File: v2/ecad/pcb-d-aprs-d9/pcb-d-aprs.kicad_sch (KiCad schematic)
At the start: 207 parts, among them K1 Omron G6K-2F-Y 5 VDC DPDT sig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, Q1 2N7002 PA_EN -> H/L low (neve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, Q2 2N7002 relay coil, Q3 2N7002, Q4 2N7002, Q5 2N7002, Q6 2N7002, Q7 2N7002, Q8 2N7002, Q9 2N7002, U1 TLV75533PDBV 3.3 V 500 mA LDO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, U10 74LVC1G08 AND: headsets AND s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, U11 74LVC1G04 inverter (2 A 4 Y):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, U12 74LVC1G08 AND: KEY = PTT_ANY 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, U13 74LVC1G04 inverter: KEY -> SA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, U14 74LVC1G08 AND: PA_KEY = KEY A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, U15 TPS22810DRV, U16 PCA9555PW 0x26: COS, PTT stat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, U2 NiceRF SA868 VHF 2 W exciter,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, U3 CP2102N-A02-GQFN28 USB-UART b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, U4 TUSB2046BI four-port USB 2.0 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, U5 USBLC6-2SC6, U6 TI PCM2912A USB audio codec (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, U7 TI TPA6132A2 headphone amplif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, U8 TLV9062IDGK dual op amp (1 OU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, U9 74LVC1G08 AND (1 A 2 B 3 GND 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, Y1 6 MHz 3225 (CL 20 pF; C1 = C2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, Y2 6 MHz 3225 (codec clock; 18 p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

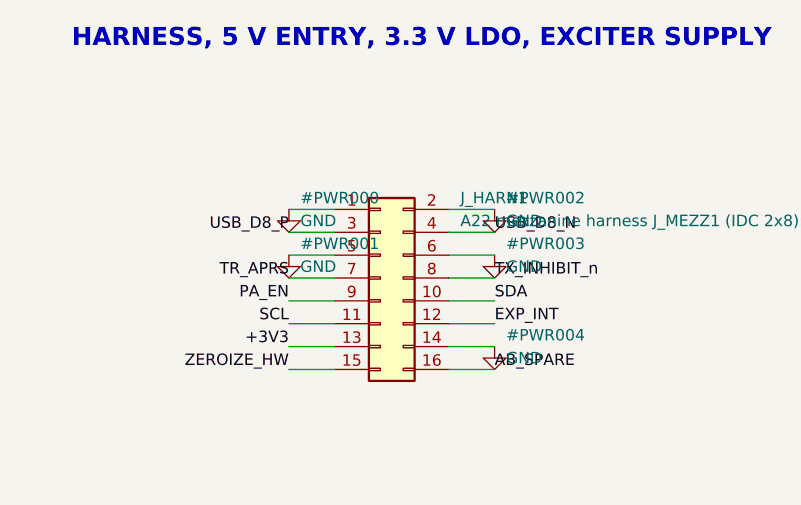
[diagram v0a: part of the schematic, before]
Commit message: feat(d): D's routed board and its regenerated schematic, tracked [MESHSAT-862]
The board is the best of the D run: 0 hard of the fifteen types, 3 unrouted
before the finish (the finish closes two of them), 5 of 5 pairs laid and
every one within 1 mm, and the schematic carries the harness pin map that
moved USB_D8 to the header's end row.

It is committed as an artefact, not as a deliverable: a routed board that
exists only in a rented box's copy directory exists nowhere, which is how
four of them were lost on 10 September. The one open and what it is are in
appendix 32.128.
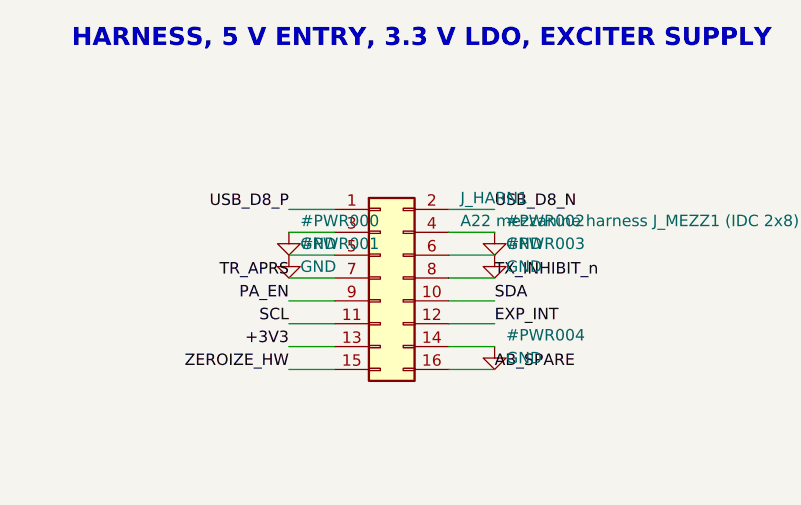
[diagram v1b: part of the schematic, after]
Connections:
- net GND: now also J_HARN1.3 (Pin_3), J_HARN1.4 (Pin_4); no longer J_HARN1.1 (Pin_1), J_HARN1.2 (Pin_2)
- net USB_D8_N: now also J_HARN1.2 (Pin_2); no longer J_HARN1.4 (Pin_4)
- net USB_D8_P: now also J_HARN1.1 (Pin_1); no longer J_HARN1.3 (Pin_3)
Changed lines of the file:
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@@
 	)
 	(wire (pts (xy 34.29 43.18) (xy 29.21 43.18)) (stroke (width 0) (type default)))
-	(symbol (lib_id "power:GND") (at 29.21 43.18 0) (unit 1) (exclude_from_sim no) (in_bom no) (on_board no) (dnp no) (fields_autoplaced yes)
-		(property "Reference" "#PWR000" (at 30.48 41.91 0) (effects (font (size 1.27 1.27)) (justify left)))
-		(property "Value" "GND" (at 30.48 44.45 0) (effects (font (size 1.27 1.27)) (justify left)))
-		(property "Footprint" "" (at 29.21 43.18 0) (effects (font (size 1.27 1.27)) (justify left) (hide yes)))
-		(property "Datasheet" "" (at 29.21 43.18 0) (effects (font (size 1.27 1.27)) (justify left) (hide yes)))
-		(property "Description" "" (at 29.21 43.18 0) (effects (font (size 1.27 1.27)) (justify left) (hide yes)))
+	(label "USB_D8_P" (at 29.21 43.18 180) (fields_autoplaced yes) (effects (font (size 1.27 1.27)) (justify right bottom)))
+	(wire (pts (xy 34.29 45.72) (xy 29.21 45.72)) (stroke (width 0) (type default)))
+	(symbol (lib_id "power:GND") (at 29.21 45.72 0) (unit 1) (exclude_from_sim no) (in_bom no) (on_board no) (dnp no) (fields_autoplaced yes)
+		(property "Reference" "#PWR000" (at 30.48 44.45 0) (effects (font (size 1.27 1.27)) (justify left)))
+		(property "Value" "GND" (at 30.48 46.99 0) (effects (font (size 1.27 1.27)) (justify left)))
+		(property "Footprint" "" (at 29.21 45.72 0) (effects (font (size 1.27 1.27)) (justify left) (hide yes)))
+		(property "Datasheet" "" (at 29.21 45.72 0) (effects (font (size 1.27 1.27)) (justify left) (hide yes)))
+		(property "Description" "" (at 29.21 45.72 0) (effects (font (size 1.27 1.27)) (justify left) (hide yes)))
 		(pin "1")
 		(instances (project "pcb-d-aprs" (path "/ba66a0ce-d686-5e81-bc86-e09a2b8c9d8d" (reference "#PWR000") (unit 1))))
 	)
-	(wire (pts (xy 34.29 45.72) (xy 29.21 45.72)) (stroke (width 0) (type default)))
-	(label "USB_D8_P" (at 29.21 45.72 180) (fields_autoplaced yes) (effects (font (size 1.27 1.27)) (justify right bottom)))
 	(wire (pts (xy 34.29 48.26) (xy 29.21 48.26)) (stroke (width 0) (type default)))
 	(symbol (lib_id "power:GND") (at 29.21 48.26 0) (unit 1) (exclude_from_sim no) (in_bom no) (on_board no) (dnp no) (fields_autoplaced yes)
@@
 	(label "ZEROIZE_HW" (at 29.21 60.96 180) (fields_autoplaced yes) (effects (font (size 1.27 1.27)) (justify right bottom)))
 	(wire (pts (xy 46.99 43.18) (xy 52.07 43.18)) (stroke (width 0) (type default)))
-	(symbol (lib_id "power:GND") (at 52.07 43.18 0) (unit 1) (exclude_from_sim no) (in_bom no) (on_board no) (dnp no) (fields_autoplaced yes)
-		(property "Reference" "#PWR002" (at 53.34 41.91 0) (effects (font (size 1.27 1.27)) (justify left)))
-		(property "Value" "GND" (at 53.34 44.45 0) (effects (font (size 1.27 1.27)) (justify left)))
-		(property "Footprint" "" (at 52.07 43.18 0) (effects (font (size 1.27 1.27)) (justify left) (hide yes)))
-		(property "Datasheet" "" (at 52.07 43.18 0) (effects (font (size 1.27 1.27)) (justify left) (hide yes)))
-		(property "Description" "" (at 52.07 43.18 0) (effects (font (size 1.27 1.27)) (justify left) (hide yes)))
+	(label "USB_D8_N" (at 52.07 43.18 0) (fields_autoplaced yes) (effects (font (size 1.27 1.27)) (justify left bottom)))
+	(wire (pts (xy 46.99 45.72) (xy 52.07 45.72)) (stroke (width 0) (type default)))
+	(symbol (lib_id "power:GND") (at 52.07 45.72 0) (unit 1) (exclude_from_sim no) (in_bom no) (on_board no) (dnp no) (fields_autoplaced yes)
+		(property "Reference" "#PWR002" (at 53.34 44.45 0) (effects (font (size 1.27 1.27)) (justify left)))
+		(property "Value" "GND" (at 53.34 46.99 0) (effects (font (size 1.27 1.27)) (justify left)))
+		(property "Footprint" "" (at 52.07 45.72 0) (effects (font (size 1.27 1.27)) (justify left) (hide yes)))
+		(property "Datasheet" "" (at 52.07 45.72 0) (effects (font (size 1.27 1.27)) (justify left) (hide yes)))
+		(property "Description" "" (at 52.07 45.72 0) (effects (font (size 1.27 1.27)) (justify left) (hide yes)))
 		(pin "1")
 		(instances (project "pcb-d-aprs" (path "/ba66a0ce-d686-5e81-bc86-e09a2b8c9d8d" (reference "#PWR002") (unit 1))))
 	)
-	(wire (pts (xy 46.99 45.72) (xy 52.07 45.72)) (stroke (width 0) (type default)))
-	(label "USB_D8_N" (at 52.07 45.72 0) (fields_autoplaced yes) (effects (font (size 1.27 1.27)) (justify left bottom)))
 	(wire (pts (xy 46.99 48.26) (xy 52.07 48.26)) (stroke (width 0) (type default)))
 	(symbol (lib_id "power:GND") (at 52.07 48.26 0) (unit 1) (exclude_from_sim no) (in_bom no) (on_board no) (dnp no) (fields_autoplaced yes)

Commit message: feat(pcb-d): D11 is cut, owner ruling 15 implemented and measured [MESHSAT-862]
0 hard, 0 unrouted, the routed-board gate ALL PASS, +5V_D8 MET, impedance 4 of 4 pairs, check_contracts 42 of
42, seventeen deliverable items, the board sha256 81614025 matching three ways.

Ruling 15 in the copper: the PWR class is back to 0.5 mm and the rail is carried at 1.7 mm (trunk) and 1.5 mm
(west branch) as locked In2 copper, sized to the current the rail's declared loads actually put in them,
1.0 A and 0.75, rather than the whole rail in one conductor. The east branch's 0.25 A is inside what the
0.5 mm class carries and needs no locked copper at all.

Ruling 9's 1.2 mm class touched 191 of the 230 pads on these nets; this touches none of them, because it is
copper and not a class width. The rail reads conductor 0.45 and pour 0.54 against their bars.
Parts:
- J_ANT: value antenna (SMA, pigtail to A22's VHF jack J_RF1) -> SMA jack: antenna pigtail to A22's VHF jack J_RF1; LCSC (none) -> C3174425
- J_HARN1: footprint Connector_IDC:IDC-Header_2x08_P2.54mm_Vertical -> meshsat:IDC-Header_2x08_P2.54mm_Vertical_NarrowPad
- J_HS1: value headset 1 lead (JST-PH 1x5 to the face plate U-174/U jack): SPK GND MIC GND PTT -> JST-PH 1x5 socket: headset 1, SPK GND MIC GND PTT (the lead runs to the face plate U-174/U jack); LCSC (none) -> C157993
- J_HS2: value headset 2 lead (JST-PH 1x5 to the face plate U-174/U jack): SPK GND MIC GND PTT -> JST-PH 1x5 socket: headset 2, SPK GND MIC GND PTT (the lead runs to the face plate U-174/U jack); LCSC (none) -> C157993
- J_PAIN: value PA drive (U.FL, coax to the RA30H1317M1 input on the plate) -> U.FL socket: PA drive (coax to the RA30H1317M1 input on the plate); LCSC (none) -> C88373
- J_PAOUT: value PA output (SMA, coax from the RA30H1317M1 output on the plate) -> SMA jack: PA output (coax from the RA30H1317M1 output on the plate); LCSC (none) -> C3174425
- J_PWR1: value 5 V from A22 J_MEZZ_PWR1 (JST-VH, 2 A eFuse on A22): + - -> JST-VH socket, 10 A: 5 V from A22 J_MEZZ_PWR1 (behind A22's 2 A eFuse U23): + -; LCSC (none) -> C274411
- J_USB3: value spare hub port 3 (JST-PH 1x4): 5V D- D+ GND -> JST-PH 1x4 socket: spare hub port 3, 5V D- D+ GND (the lead is made up at build); LCSC (none) -> C131334
- J_VGG: value PA gate bias lead (JST-PH 1x2 to the RA30H1317M1 VGG): VGG GND -> JST-PH 1x2 socket: PA gate bias, VGG GND (the lead runs to the RA30H1317M1 VGG pin); LCSC (none) -> C5251182
- LED1, LED3, LED6: LCSC (none) -> C12624
- LED2, LED5: LCSC (none) -> C2287
- LED4: LCSC (none) -> C2286

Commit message: feat(ecad): readable schematics: a page engine draws every board as wired A3 pages of functional blocks (ICs as boxes with rails top and grounds bottom, passives on the pins they serve, decoupling rows, power symbols), proves the drawing's connectivity before writing, and the build cuts the sheet into A3 pages; all six netlists identical; the render scene puts the lit display on the glass and the monitor's rear block under it [MESHSAT-862]
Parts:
- removed C1: 47u 6.3V X5R 1210, Capacitor_SMD:C_1210_3225Metric, symbol Device:C
- removed C15, C56, C57, C63: 100n, Capacitor_SMD:C_0603_1608Metric, symbol Device:C
- removed C34, C37, C38: 1u, Capacitor_SMD:C_0603_1608Metric, symbol Device:C
- removed J_VGG: JST-PH 1x2 socket: PA gate bias, VGG GND (the lea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, Connector_JST:JST_PH_B2B-PH-K_1x02_P2.00mm_Vertical, symbol Connector_Generic:Conn_01x02
- removed L1: 68nH 0805 (LPF, 145 MHz 5th order; values to be v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, Inductor_SMD:L_0805_2012Metric, symbol Device:L
- removed R19: 15k, Resistor_SMD:R_0603_1608Metric, symbol Device:R
- removed R34: 100k, Resistor_SMD:R_0603_1608Metric, symbol Device:R
- removed R41: 4.7k, Resistor_SMD:R_0603_1608Metric, symbol Device:R
- removed R56: 27 1% 2010, Resistor_SMD:R_2010_5025Metric, symbol Device:R
- removed R66, R71, R9: 10k, Resistor_SMD:R_0603_1608Metric, symbol Device:R
- removed U1: TLV75533PDBV 3.3 V 500 mA LDO (1 IN 2 GND 3 EN 4 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, Package_TO_SOT_SMD:SOT-23-5, symbol Connector_Generic:Conn_01x05
- removed U10: 74LVC1G08 AND: headsets AND software PTT (RTS), Package_TO_SOT_SMD:SOT-23-5, symbol Connector_Generic:Conn_01x05
- removed U11: 74LVC1G04 inverter (2 A 4 Y): PTT_ANY, Package_TO_SOT_SMD:SOT-23-5, symbol Connector_Generic:Conn_01x05
- removed U12: 74LVC1G08 AND: KEY = PTT_ANY AND TX_INHIBIT_n (th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, Package_TO_SOT_SMD:SOT-23-5, symbol Connector_Generic:Conn_01x05
- removed U13: 74LVC1G04 inverter: KEY -> SA868 PTT (low = trans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, Package_TO_SOT_SMD:SOT-23-5, symbol Connector_Generic:Conn_01x05
- removed U14: 74LVC1G08 AND: PA_KEY = KEY AND PA_EN (A22's PA r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, Package_TO_SOT_SMD:SOT-23-5, symbol Connector_Generic:Conn_01x05
- removed U9: 74LVC1G08 AND (1 A 2 B 3 GND 4 Y 5 VCC): both hea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, Package_TO_SOT_SMD:SOT-23-5, symbol Connector_Generic:Conn_01x05
- added C14: 27p NP0, Capacitor_SMD:C_0402_1005Metric, symbol Device:C
- added C23: 1u, Capacitor_SMD:C_0603_1608Metric, symbol Device:C
- added C3: 10u, Capacitor_SMD:C_0805_2012Metric, symbol Device:C
- added C52: 100n, Capacitor_SMD:C_0603_1608Metric, symbol Device:C
- added K1: Omron G6K-2F-Y 5 VDC DPDT signal relay, T/R, Relay_SMD:Relay_DPDT_Omron_G6K-2F-Y, symbol Relay:G6K-2
- added L2: 68nH 0805 (LPF), Inductor_SMD:L_0805_2012Metric, symbol Device:L
- added Q8, Q9: 2N7002, Package_TO_SOT_SMD:SOT-23, symbol Transistor_FET:2N7002
- added R13: 22, Resistor_SMD:R_0603_1608Metric, symbol Device:R
- added R38, R46, R69: 10k, Resistor_SMD:R_0603_1608Metric, symbol Device:R
- added TP15: TX_INHIBIT_n, TestPoint:TestPoint_Pad_D1.5mm, symbol Connector:TestPoint
- added U1: TLV75533PDBV 3.3 V 500 mA LDO (1 IN 2 GND 3 EN 4 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, Package_TO_SOT_SMD:SOT-23-5, symbol meshsat_ic:U1
- added U10: 74LVC1G08 AND: headsets AND software PTT (RTS), Package_TO_SOT_SMD:SOT-23-5, symbol meshsat_ic:U10
- added U11: 74LVC1G04 inverter (2 A 4 Y): PTT_ANY, Package_TO_SOT_SMD:SOT-23-5, symbol meshsat_ic:U11
- added U12: 74LVC1G08 AND: KEY = PTT_ANY AND TX_INHIBIT_n (th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, Package_TO_SOT_SMD:SOT-23-5, symbol meshsat_ic:U12
- added U13: 74LVC1G04 inverter: KEY -> SA868 PTT (low = trans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, Package_TO_SOT_SMD:SOT-23-5, symbol meshsat_ic:U13
- added U14: 74LVC1G08 AND: PA_KEY = KEY AND PA_EN (A22's PA r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, Package_TO_SOT_SMD:SOT-23-5, symbol meshsat_ic:U14
- added U15: TPS22810DRV, Package_SON:WSON-6-1EP_2x2mm_P0.65mm_EP1x1.6mm, symbol Power_Management:TPS22810DRV
- added U4: TUSB2046BI four-port USB 2.0 full-speed hub (LQFP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, Package_QFP:LQFP-32_7x7mm_P0.8mm, symbol Connector_Generic:TUSB2046B
- added U8: TLV9062IDGK dual op amp (1 OUT1 2 IN1- 3 IN1+ 4 V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, Package_SO:VSSOP-8_3x3mm_P0.65mm, symbol meshsat_ic:U8
- added Y1: 6 MHz 3225 (CL 20 pF; C1 = C2 = 27 pF and Rd 1.5k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, Crystal:Crystal_SMD_3225-4Pin_3.2x2.5mm, symbol Device:Crystal_GND24
- added Y2: 6 MHz 3225 (codec clock; 18 pF loads, to confirm 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, Crystal:Crystal_SMD_3225-4Pin_3.2x2.5mm, symbol Device:Crystal_GND24
- C1: renamed from C3; value 10u -> 47u 6.3V X5R 1210; footprint Capacitor_SMD:C_0805_2012Metric -> Capacitor_SMD:C_1210_3225Metric
- C15: renamed from R13; value 22 -> 100n; footprint Resistor_SMD:R_0603_1608Metric -> Capacitor_SMD:C_0603_1608Metric; symbol Device:R -> Device:C
- C37: renamed from U8; value TLV9062IDGK dual op amp (1 OUT1 2 IN1- 3 IN1+ 4 V- 5 IN2+ 6 IN2- 7 OUT2 8 V+): A the mic sum, B unused as a follower -> 1u; footprint Package_SO:VSSOP-8_3x3mm_P0.65mm -> Capacitor_SMD:C_0603_1608Metric; symbol Connector_Generic:Conn_01x08 -> Device:C
- C38: renamed from R38; value 10k -> 1u; footprint Resistor_SMD:R_0603_1608Metric -> Capacitor_SMD:C_0603_1608Metric; symbol Device:R -> Device:C
- C56: renamed from R69; value 10k -> 100n; footprint Resistor_SMD:R_0603_1608Metric -> Capacitor_SMD:C_0603_1608Metric; symbol Device:R -> Device:C
- C57: renamed from K1; value Omron G6K-2F-Y 5 VDC DPDT signal relay, T/R -> 100n; footprint Relay_SMD:Relay_DPDT_Omron_G6K-2F-Y -> Capacitor_SMD:C_0603_1608Metric; symbol Relay:G6K-2 -> Device:C
- C63: renamed from Q9; value 2N7002 -> 100n; footprint Package_TO_SOT_SMD:SOT-23 -> Capacitor_SMD:C_0603_1608Metric; symbol Transistor_FET:2N7002 -> Device:C; LCSC C8545 -> (none)
- J_VGG: renamed from U4; value TUSB2046BI four-port USB 2.0 full-speed hub (LQFP-32; BUSPWR low = self-powered, EXTMEM high, GANGED high, TSTMODE low) -> JST-PH 1x2 socket: PA gate bias, VGG GND (the lead runs to the RA30H1317M1 VGG pin); footprint Package_QFP:LQFP-32_7x7mm_P0.8mm -> Connector_JST:JST_PH_B2B-PH-K_1x02_P2.00mm_Vertical; symbol Connector_Generic:TUSB2046B -> Connector_Generic:Conn_01x02; LCSC (none) -> C5251182
- L1: renamed from U15; value TPS22810DRV -> 68nH 0805 (LPF, 145 MHz 5th order; values to be verified in MESHSAT-818); footprint Package_SON:WSON-6-1EP_2x2mm_P0.65mm_EP1x1.6mm -> Inductor_SMD:L_0805_2012Metric; symbol Power_Management:TPS22810DRV -> Device:L
- R19: renamed from C14; value 27p NP0 -> 15k; footprint Capacitor_SMD:C_0402_1005Metric -> Resistor_SMD:R_0603_1608Metric; symbol Device:C -> Device:R
- R34: renamed from Y2; value 6 MHz 3225 (codec clock; 18 pF loads, to confirm on the EVM sheet) -> 100k; footprint Crystal:Crystal_SMD_3225-4Pin_3.2x2.5mm -> Resistor_SMD:R_0603_1608Metric; symbol Device:Crystal_GND24 -> Device:R
- R41: renamed from R46; value 10k -> 4.7k
- R56: renamed from L2; value 68nH 0805 (LPF) -> 27 1% 2010; footprint Inductor_SMD:L_0805_2012Metric -> Resistor_SMD:R_2010_5025Metric; symbol Device:L -> Device:R
- R66: renamed from TP15; value TX_INHIBIT_n -> 10k; footprint TestPoint:TestPoint_Pad_D1.5mm -> Resistor_SMD:R_0603_1608Metric; symbol Connector:TestPoint -> Device:R; now in the parts list
- R71: renamed from Q8; value 2N7002 -> 10k; footprint Package_TO_SOT_SMD:SOT-23 -> Resistor_SMD:R_0603_1608Metric; symbol Transistor_FET:2N7002 -> Device:R; LCSC C8545 -> (none)
- R9: renamed from Y1; value 6 MHz 3225 (CL 20 pF; C1 = C2 = 27 pF and Rd 1.5k per SLLS413 figure 6) -> 10k; footprint Crystal:Crystal_SMD_3225-4Pin_3.2x2.5mm -> Resistor_SMD:R_0603_1608Metric; symbol Device:Crystal_GND24 -> Device:R
- U9: renamed from C52; value 100n -> 74LVC1G08 AND (1 A 2 B 3 GND 4 Y 5 VCC): both headset PTT lines idle high; footprint Capacitor_SMD:C_0603_1608Metric -> Package_TO_SOT_SMD:SOT-23-5; symbol Device:C -> meshsat_ic:U9
- renumbered C23 to C34
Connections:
- net +3V3: now also C63.1, R71.2, R69.2; no longer C56.2
- net +3V3_D8: now also C15.1, C56.1, R66.2, R9.2, U9.5 (+3V3_D8), C52.1, Q8.1 (G), Q9.1 (G), U1.5 (+3V3_D8), U10.5 (+3V3_D8), U11.5 (+3V3_D8), U12.5 (+3V3_D8), U13.5 (+3V3_D8), U14.5 (+3V3_D8), U4.25 (VCC), U4.26 (EXTMEM), U4.3 (VCC), U4.6 (EEDATA/GANGED); no longer C63.1 (G), J_VGG.25 (VCC), J_VGG.26 (EXTMEM), J_VGG.3 (VCC), J_VGG.6 (EEDATA/GANGED), R71.1 (G), U9.1
- net +5V_D8: now also C3.1, K1.1, R38.1, U1.1 (+5V_D8), U1.3 (+5V_D8), U15.6 (VIN), U8.8 (+5V_D8); no longer C37.8 (Pin_8), C38.1, L1.6 (VIN)
- net AMP_EN: now also Q9.2 (S); no longer C63.2 (S)
- net AMP_INL_N: now also C37.1
- net AMP_INR_N: now also C38.1
- net GND: now also C15.2, C37.2, C38.2, C56.2, C57.2, C63.2, J_VGG.2 (Pin_2), U9.3 (GND), C14.2, C23.2, C3.2, C52.2, U1.2 (GND), U10.3 (GND), U11.3 (GND), U12.3 (GND), U13.3 (GND), U14.3 (GND), U15.4 (GND), U15.7 (GND), U4.27 (TSTPLL/48MCLK), U4.28 (GND), U4.31 (TSTMODE), U4.7 (GND), U4.8 (BUSPWR), U8.4 (GND), Y1.2 (G), Y1.4 (G), Y2.2 (G), Y2.4 (G); no longer C34.2, C37.4 (Pin_4), J_VGG.27 (TSTPLL/48MCLK), J_VGG.28 (GND), J_VGG.31 (TSTMODE), J_VGG.7 (GND), J_VGG.8 (BUSPWR), L1.4 (GND), L1.7 (GND), R34.4 (G), R9.2 (G), R9.4 (G), U9.2
- net HS2_MIC_AC: now also R41.1
- net HUB_DM0: now also U4.2 (DM0); no longer J_VGG.2 (DM0)
- net HUB_DM1: now also R13.1, U4.11 (DM1); no longer C15.1, J_VGG.11 (DM1)
- net HUB_DM2: now also U4.15 (DM2); no longer J_VGG.15 (DM2)
- net HUB_DM3: now also U4.19 (DM3); no longer J_VGG.19 (DM3)
- net HUB_DM4: now also U4.23 (DM4); no longer J_VGG.23 (DM4)
- net HUB_DP0: now also U4.1 (DP0); no longer J_VGG.1 (DP0)
- net HUB_DP1: now also U4.12 (DP1); no longer J_VGG.12 (DP1)
- net HUB_DP2: now also U4.16 (DP2); no longer J_VGG.16 (DP2)
- net HUB_DP3: now also U4.20 (DP3); no longer J_VGG.20 (DP3)
- net HUB_DP4: now also U4.24 (DP4); no longer J_VGG.24 (DP4)
- net HUB_OVRCUR_n: now also R9.1, U4.10 (OVRCUR1_n), U4.14 (OVRCUR2_n), U4.18 (OVRCUR3_n), U4.22 (OVRCUR4_n); no longer J_VGG.10 (OVRCUR1_n), J_VGG.14 (OVRCUR2_n), J_VGG.18 (OVRCUR3_n), J_VGG.22 (OVRCUR4_n)
- net HUB_RST_n: now also U4.4 (RESET_n); no longer J_VGG.4 (RESET_n)
- net HUB_XTAL1: now also U4.30 (XTAL1), Y1.1; no longer J_VGG.30 (XTAL1), R9.1
- net HUB_XTAL2: now also U4.29 (XTAL2); no longer J_VGG.29 (XTAL2)
- net HUB_XTAL2R: now also C14.1, Y1.3; no longer R19.1, R9.3
- net KEY: now also U12.4 (KEY), U13.2 (KEY), U14.1 (KEY)
- net MICAMP_IN_N: now also R41.2, U8.2 (MICAMP_IN_N); no longer C37.2 (Pin_2)
- net MICAMP_OUT: now also U8.1 (MICAMP_OUT); no longer C37.1 (Pin_1)
- net MIC_SUM: now also R46.2; no longer R41.2
- net MMUTE: now also R34.1
- net OPB_OUT: now also U8.6 (OPB_OUT), U8.7 (OPB_OUT); no longer C37.6 (Pin_6), C37.7 (Pin_7)
- net PA_EN: now also U14.2 (PA_EN)
- net PA_KEY: now also U14.4 (PA_KEY), U15.5 (EN/UVLO); no longer L1.5 (EN/UVLO)
- net PCM_L_AC: now also C34.2
- net PCM_R_AC: now also R46.1; no longer R41.1
- net PCM_VCCP: now also C23.1; no longer C34.1
- net PCM_VOUTL: now also C34.1
- net PCM_XTI: now also Y2.1; no longer R34.1
- net PCM_XTO: now also Y2.3; no longer R34.3
- net PTT_ANY: now also U11.4 (PTT_ANY), U12.1 (PTT_ANY)
- net PTT_ANY_n: now also U10.4 (PTT_ANY_n), U11.2 (PTT_ANY_n)
- net PTT_HS1_n: now also U9.1 (PTT_HS1_n)
- net PTT_HS2_n: now also U9.2 (PTT_HS2_n)
- net PTT_HS_n: now also U9.4 (PTT_HS_n), U10.1 (PTT_HS_n)
- net PTT_SW_n: now also U10.2 (PTT_SW_n)
- net RF_ANT: now also K1.6; no longer C57.6
- net RF_DRV: now also R56.2
- net RF_LPF_M: now also L1.2, L2.1; no longer R56.1
- net RF_LPF_OUT: now also K1.5, L2.2; no longer C57.5, R56.2
- net RF_PAD_IN: now also K1.4; no longer C57.4
- net RF_PAD_M: now also R56.1
- net RF_PAOUT: now also L1.1
- net RF_RX: now also K1.2, K1.7; no longer C57.2, C57.7
- net RF_SA: now also K1.3; no longer C57.3
- net RLY_K: now also K1.8; no longer C57.8
- net SA_AUDIO_ON_n: now also R66.1
- net SA_PD: now also Q8.2 (S); no longer R71.2 (S)
- net SA_PTT_n: now also U13.4 (SA_PTT_n)
- net TX_INHIBIT_n: now also TP15.1, U12.2 (TX_INHIBIT_n); no longer R66.1
- net USB1_N: now also R13.2; no longer C15.2
- net USB2_N: now also R19.1
- net VGG_CT: now also U15.3 (CT); no longer L1.3 (CT)
- net VGG_SW: now also J_VGG.1 (Pin_1), U15.1 (VOUT); no longer L1.1 (VOUT)
- net VREF: now also R38.2, U8.3 (VREF), U8.5 (VREF); no longer C37.3 (Pin_3), C37.5 (Pin_5), C38.2
- net X_AMP_EN: now also Q9.3 (D); no longer C63.3 (D)
- net X_PTT_HS1_n: now also R69.1; no longer C56.1
- net X_PTT_HS2_n: now also R71.1
- net X_SA_PD: now also Q8.3 (D); no longer R71.3 (D)
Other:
- note added: "22p 500V"
- note added: "27 1%"
- note added: "2N7002 PA_EN -> H/L low"
- note added: "39p 500V"
- note added: "47u 6.3V"
- note added: "6 MHz 3225"
- note added: "600R 2A"
- note added: "68nH 0805"
- note added: "74LVC1G04 inverter"
- note added: "74LVC1G08 AND"
- note added: "A22 mezzanine harness J_MEZZ1"
- note added: "CP2102N-A02-GQFN28 USB-UART bridge"
- note added: "HARNESS, 5 V ENTRY, 3.3 V LDO, EXCITER SUPPLY | SA868 EXCITER, UART BRIDGE, T/R RELAY, 10 dB PAD, LPF, PA LEADS, GATE BIAS SWITCH"
- note added: "JST-PH 1x2 socket"
- note added: "JST-PH 1x4 socket"
- note added: "JST-PH 1x5 socket"
- note added: "JST-VH socket"
- note added: "NiceRF SA868 VHF 2 W exciter"
- note added: "Omron G6K-2F-Y 5 VDC DPDT signal r.."
- note added: "PCA9555PW 0x26"
- note added: "PCB-D APRS MEZZANINE D11"
- note added: "PTT AND EMCON LOGIC, PTT MIRROR, LEDS, EXPANDER 0x26 WITH LEVEL STAGES, TEST POINTS, FLAGS (continued)"
- note added: "SA868 EXCITER, UART BRIDGE, T/R RELAY, 10 dB PAD, LPF, PA LEADS, GATE BIAS SWITCH (continued)"
- note added: "SA868 EXCITER, UART BRIDGE, T/R RELAY, 10 dB PAD, LPF, PA LEADS, GATE BIAS SWITCH | USB HUB TUSB2046B, PORT TERMINATIONS, SPARE PORT"
- note added: "SMA jack"
- note added: "TI PCM2912A USB audio codec"
- note added: "TI TPA6132A2 headphone amplifier"
- note added: "TLV75533PDBV 3.3 V 500 mA LDO"
- note added: "TLV9062IDGK dual op amp"
- note added: "TUSB2046BI four-port USB 2.0 full-.."
- note added: "U.FL socket"
- note added: "USB AUDIO CODEC PCM2912A, HEADPHONE AMPLIFIER, MIC PREAMP, HEADSET LEADS (continued)"
- note added: "USB AUDIO CODEC PCM2912A, HEADPHONE AMPLIFIER, MIC PREAMP, HEADSET LEADS | PTT AND EMCON LOGIC, PTT MIRROR, LEDS, EXPANDER 0x26 WITH LEVEL STAGES, TEST POINTS, FLAGS"
- note added: "decoupling of U6"
- note added: "decoupling of U7"
- note added: "decoupling of U8"
- note added: "electret bias headset 1"
- note added: "green receive"
- note added: "page 1 of 5 MeshSat field kit V2, CERN-OHL-S-2.0 PROTOTYPE, nothing built 2026-09-15"
- note added: "page 2 of 5 MeshSat field kit V2, CERN-OHL-S-2.0 PROTOTYPE, nothing built 2026-09-15"
- note added: "page 3 of 5 MeshSat field kit V2, CERN-OHL-S-2.0 PROTOTYPE, nothing built 2026-09-15"
- note added: "page 4 of 5 MeshSat field kit V2, CERN-OHL-S-2.0 PROTOTYPE, nothing built 2026-09-15"
- note added: "page 5 of 5 MeshSat field kit V2, CERN-OHL-S-2.0 PROTOTYPE, nothing built 2026-09-15"
- moved on the sheet: C1, C34, R41

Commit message: feat(ecad): the schematic pages draw every net that stays on a page as wires between its parts and mark every signal that leaves a page with the pages it goes to; B's shared area is sectioned by its generator headings; six netlists identical [MESHSAT-862]
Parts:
- removed C12, C22, C30, C31: 1u, Capacitor_SMD:C_0603_1608Metric, symbol Device:C
- removed C43: 100p NP0, Capacitor_SMD:C_0402_1005Metric, symbol Device:C
- removed C63: 100n, Capacitor_SMD:C_0603_1608Metric, symbol Device:C
- removed J_USB3: JST-PH 1x4 socket: spare hub port 3, 5V D- D+ GND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, Connector_JST:JST_PH_B4B-PH-K_1x04_P2.00mm_Vertical, symbol Connector_Generic:Conn_01x04
- removed R27: 33, Resistor_SMD:R_0603_1608Metric, symbol Device:R
- removed R50: 1k, Resistor_SMD:R_0603_1608Metric, symbol Device:R
- removed R7: 22, Resistor_SMD:R_0603_1608Metric, symbol Device:R
- removed R74: 10k, Resistor_SMD:R_0603_1608Metric, symbol Device:R
- removed R8: 1.5k, Resistor_SMD:R_0603_1608Metric, symbol Device:R
- removed Y1: 6 MHz 3225 (CL 20 pF; C1 = C2 = 27 pF and Rd 1.5k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, Crystal:Crystal_SMD_3225-4Pin_3.2x2.5mm, symbol Device:Crystal_GND24
- removed Y2: 6 MHz 3225 (codec clock; 18 pF loads, to confirm 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, Crystal:Crystal_SMD_3225-4Pin_3.2x2.5mm, symbol Device:Crystal_GND24
- added C13: 27p NP0, Capacitor_SMD:C_0402_1005Metric, symbol Device:C
- added C32, C36: 1u, Capacitor_SMD:C_0603_1608Metric, symbol Device:C
- added C33: 10u, Capacitor_SMD:C_0805_2012Metric, symbol Device:C
- added C39: 100n, Capacitor_SMD:C_0603_1608Metric, symbol Device:C
- added Q5: 2N7002, Package_TO_SOT_SMD:SOT-23, symbol Transistor_FET:2N7002
- added R16: 22, Resistor_SMD:R_0603_1608Metric, symbol Device:R
- added R23, R24: 15k, Resistor_SMD:R_0603_1608Metric, symbol Device:R
- added R47, R75, R77: 10k, Resistor_SMD:R_0603_1608Metric, symbol Device:R
- added U6: TI PCM2912A USB audio codec (TQFP-32): mono input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, Package_QFP:TQFP-32_7x7mm_P0.8mm, symbol Connector_Generic:PCM2912A
- added U7: TI TPA6132A2 headphone amplifier (QFN-16), receiv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, Package_DFN_QFN:QFN-16-1EP_3x3mm_P0.5mm_EP1.75x1.75mm, symbol Connector_Generic:TPA6132A2
- C12: renamed from R16; value 22 -> 1u; footprint Resistor_SMD:R_0603_1608Metric -> Capacitor_SMD:C_0603_1608Metric; symbol Device:R -> Device:C
- C22: renamed from U7; value TI TPA6132A2 headphone amplifier (QFN-16), receive audio to the two headset leads -> 1u; footprint Package_DFN_QFN:QFN-16-1EP_3x3mm_P0.5mm_EP1.75x1.75mm -> Capacitor_SMD:C_0603_1608Metric; symbol Connector_Generic:TPA6132A2 -> Device:C
- C31: renamed from C33; value 10u -> 1u; footprint Capacitor_SMD:C_0805_2012Metric -> Capacitor_SMD:C_0603_1608Metric
- C43: renamed from C39; value 100n -> 100p NP0; footprint Capacitor_SMD:C_0603_1608Metric -> Capacitor_SMD:C_0402_1005Metric
- C63: renamed from Q5; value 2N7002 -> 100n; footprint Package_TO_SOT_SMD:SOT-23 -> Capacitor_SMD:C_0603_1608Metric; symbol Transistor_FET:2N7002 -> Device:C; LCSC C8545 -> (none)
- J_USB3: renamed from U6; value TI PCM2912A USB audio codec (TQFP-32): mono input from the exciter, stereo output to the headphone amplifier and the tr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 -> JST-PH 1x4 socket: spare hub port 3, 5V D- D+ GND (the lead is made up at build); footprint Package_QFP:TQFP-32_7x7mm_P0.8mm -> Connector_JST:JST_PH_B4B-PH-K_1x04_P2.00mm_Vertical; symbol Connector_Generic:PCM2912A -> Connector_Generic:Conn_01x04; LCSC (none) -> C131334
- R17: renamed from C13; value 27p NP0 -> 22; footprint Capacitor_SMD:C_0402_1005Metric -> Resistor_SMD:R_0603_1608Metric; symbol Device:C -> Device:R
- R27: renamed from R47; value 10k -> 33
- R50: renamed from R75; value 10k -> 1k
- R8: renamed from R14; value 15k -> 1.5k
- Y1: renamed from R23; value 15k -> 6 MHz 3225 (CL 20 pF; C1 = C2 = 27 pF and Rd 1.5k per SLLS413 figure 6); footprint Resistor_SMD:R_0603_1608Metric -> Crystal:Crystal_SMD_3225-4Pin_3.2x2.5mm; symbol Device:R -> Device:Crystal_GND24
- Y2: renamed from C36; value 1u -> 6 MHz 3225 (codec clock; 18 pF loads, to confirm on the EVM sheet); footprint Capacitor_SMD:C_0603_1608Metric -> Crystal:Crystal_SMD_3225-4Pin_3.2x2.5mm; symbol Device:C -> Device:Crystal_GND24
- renumbered C32 to C30, R24 to R14, R17 to R7, R77 to R74
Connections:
- net +3V3: now also C63.1, R75.2, R77.2; no longer R50.2, R74.2
- net +3V3_D8: now also R74.2, R8.2, Q5.1 (G), U7.6 (G0); no longer C22.6 (G0), C63.1 (G)
- net +5V_D8: now also J_USB3.1 (Pin_1), C32.1, C33.1, C39.1, U6.2 (VBUS), U7.14 (VDD); no longer C22.14 (VDD), C30.1, C31.1, C43.1, J_USB3.2 (VBUS)
- net AMP_CPN: now also C30.2, U7.9 (CPN); no longer C22.9 (CPN)
- net AMP_CPP: now also C30.1, U7.11 (CPP); no longer C22.11 (CPP)
- net AMP_EN: now also U7.13 (EN); no longer C22.13 (EN)
- net AMP_HPVDD: now also C31.1, U7.12 (HPVDD); no longer C22.12 (HPVDD)
- net AMP_HPVSS: now also U7.8 (HPVSS); no longer C22.8 (HPVSS)
- net AMP_INL_N: now also U7.1 (INL-); no longer C22.1 (INL-)
- net AMP_INL_P: now also U7.2 (INL+); no longer C22.2 (INL+)
- net AMP_INR_N: now also U7.4 (INR-); no longer C22.4 (INR-)
- net AMP_INR_P: now also C36.2, U7.3 (INR+); no longer C22.3 (INR+), Y2.2
- net GND: now also C12.2, C22.2, C63.2, J_USB3.4 (Pin_4), Y1.4 (G), Y2.2 (G), Y2.4 (G), C13.2, C32.2, C33.2, C39.2, R23.2, R24.2, R47.2, U6.1 (BGND), U6.13 (AGND), U6.20 (HGND), U6.23 (MAMP), U6.24 (POWER), U6.25 (PGND), U6.28 (TEST0), U6.6 (DGND), U7.10 (PGND), U7.15 (SGND), U7.17 (PAD), U7.7 (G1); no longer C22.10 (PGND), C22.15 (SGND), C22.17 (PAD), C22.7 (G1), C30.2, C43.2, J_USB3.1 (BGND), J_USB3.13 (AGND), J_USB3.20 (HGND), J_USB3.23 (MAMP), J_USB3.24 (POWER), J_USB3.25 (PGND), J_USB3.28 (TEST0), J_USB3.6 (DGND), R17.2, R27.2, R8.2
- net HS1_SPK: now also U7.16 (OUTL); no longer C22.16 (OUTL)
- net HS2_SPK: now also U7.5 (OUTR); no longer C22.5 (OUTR)
- net HUB_DM0: now also R7.2
- net HUB_DM2: now also R17.1; no longer R7.1
- net HUB_DP0: now also R8.1
- net HUB_DP2: now also R16.1; no longer C12.1
- net HUB_DP4: now also R24.1; no longer R14.1
- net HUB_RST_n: now also C12.1
- net HUB_XTAL1: now also Y1.1, C13.1; no longer R17.1
- net HUB_XTAL2R: now also Y1.3
- net LED_PA_A: now also R50.2
- net LED_PLAY_K: now also U6.32 (PLAY); no longer J_USB3.32 (PLAY)
- net LED_REC_K: now also U6.31 (REC); no longer J_USB3.31 (REC)
- net MICAMP_IN_N: now also C43.2
- net MICAMP_OUT: now also C43.1
- net MIC_SUM: now also R47.1; no longer R27.1
- net MMUTE: now also U6.30 (MMUTE); no longer J_USB3.30 (MMUTE)
- net PA_KEY: now also R50.1, R74.1
- net PCM_VCCA: now also U6.15 (VCCA); no longer J_USB3.15 (VCCA)
- net PCM_VCCL: now also U6.19 (VCCL); no longer J_USB3.19 (VCCL)
- net PCM_VCCP: now also U6.26 (VCCP); no longer J_USB3.26 (VCCP)
- net PCM_VCCR: now also C22.1, U6.21 (VCCR); no longer J_USB3.21 (VCCR)
- net PCM_VCOM1: now also U6.11 (VCOM1); no longer J_USB3.11 (VCOM1)
- net PCM_VCOM2: now also U6.12 (VCOM2); no longer J_USB3.12 (VCOM2)
- net PCM_VDD: now also U6.27 (TEST1), U6.5 (VDD); no longer J_USB3.27 (TEST1), J_USB3.5 (VDD)
- net PCM_VIN: now also U6.16 (VIN); no longer J_USB3.16 (VIN)
- net PCM_VOUTL: now also U6.18 (VOUTL); no longer J_USB3.18 (VOUTL)
- net PCM_VOUTR: now also U6.22 (VOUTR); no longer J_USB3.22 (VOUTR)
- net PCM_XTI: now also Y2.1, U6.8 (XTI); no longer J_USB3.8 (XTI)
- net PCM_XTO: now also Y2.3, U6.7 (XTO); no longer J_USB3.7 (XTO)
- net PTT_HS2_n: now also Q5.2 (S); no longer C63.2 (S)
- net RX_MIX: now also C36.1; no longer Y2.1
- net USB1_N: now also R27.1
- net USB1_NR: now also R27.2, U6.3 (D-); no longer J_USB3.3 (D-)
- net USB1_P: now also R14.1; no longer R8.1
- net USB1_PR: now also U6.4 (D+); no longer J_USB3.4 (D+)
- net USB2_N: now also R17.2; no longer R7.2
- net USB2_P: now also R16.2; no longer C12.2
- net USB3_N: now also J_USB3.2 (Pin_2), R23.1; no longer Y1.1
- net USB3_P: now also J_USB3.3 (Pin_3)
- net USB_D8_N: now also R7.1
- net X_PA_KEY: now also R75.1; no longer R50.1
- net X_PTT_HS2_n: now also Q5.3 (D); no longer C63.3 (D)
- net X_SA_PD: now also R77.1; no longer R74.1
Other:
- note added: "p1"
- note added: "p1,3"
- note added: "p1,4"
- note added: "p1,5"
- note added: "p2"
- note added: "p2,4"
- note added: "p2,5"
- note added: "p3"
- note added: "p3,5"
- note added: "p4"
- note added: "p4,5"
- note added: "p5"
- note removed: "decoupling of U7"
- note removed: "decoupling of U8"
- moved on the sheet: C30, C31, C43, C58, C59, J_ANT, J_PAOUT, L1, R14, R27, R50, R56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
